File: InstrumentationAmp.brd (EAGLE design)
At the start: 21 x 23.5 mm, 14 parts, among them IC1 AD623R

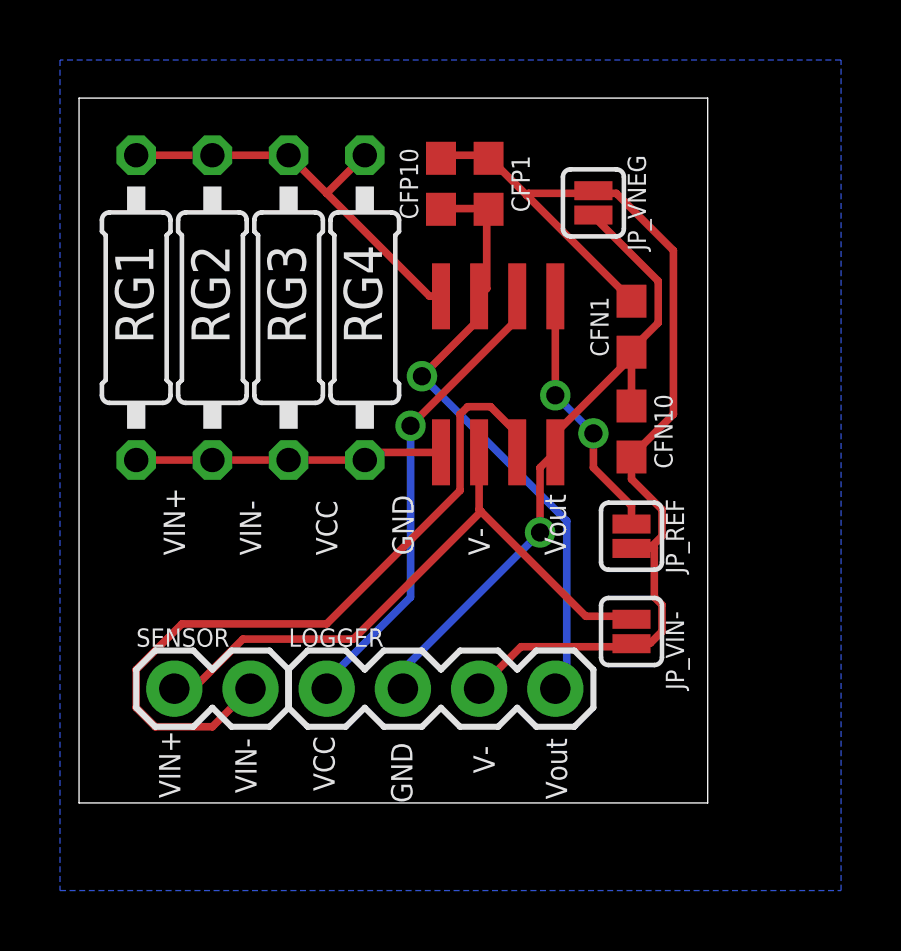
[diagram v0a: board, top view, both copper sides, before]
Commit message: Names match README; connect Vref
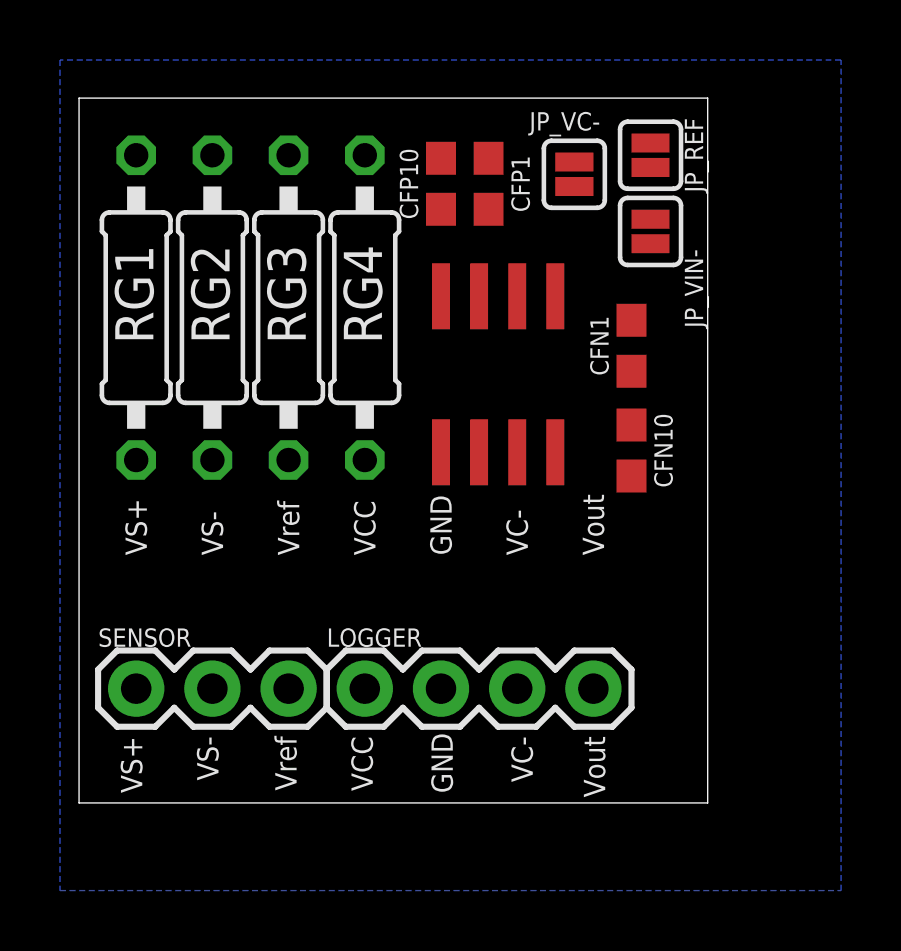
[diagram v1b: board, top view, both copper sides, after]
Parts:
- removed JP_VNEG: (no value), SparkFun-Jumpers:SMT-JUMPER_2_NC_PASTE_SILK
- added JP_VC-: (no value), SparkFun-Jumpers:SMT-JUMPER_2_NC_PASTE_SILK
- SENSOR: device SparkFun-Connectors:1X02 -> SparkFun-Connectors:1X03
- moved JP_VIN- 13.4 mm to (19.1, 19.1)
- moved JP_REF 12.7 mm to (19.1, 21.6)
- moved SENSOR 1.27 mm to (1.91, 3.81)
- moved LOGGER 1.27 mm to (9.53, 3.81)
- moved CFN1 0.63 mm to (18.4, 15.2)
- moved CFN10 0.63 mm to (18.4, 11.7)
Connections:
- removed net N$3: IC1.5, JP_REF.2
- removed net VIN+: IC1.3, SENSOR.2
- removed net VIN-: IC1.2, JP_VIN-.2, SENSOR.1
- new net VREF: IC1.5, JP_REF.2, SENSOR.1
- new net VS+: IC1.3, SENSOR.3
- new net VS-: IC1.2, JP_VIN-.2, SENSOR.2
- net GND: now also JP_VC-.1; no longer JP_VNEG.1
- net VNEG: now also JP_VC-.2; no longer JP_VNEG.2
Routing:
- net GND: track 36.0 -> 0.00 mm
- net VIN+: track 24.7 -> 0.00 mm
- net VNEG: track 21.9 -> 0.00 mm, vias 1 -> 0
- net VIN-: track 21.2 -> 0.00 mm
- net VCC: track 20.7 -> 0.00 mm, vias 1 -> 0
- net VOUT: track 15.7 -> 0.00 mm, vias 1 -> 0
- net RG-B: track 13.9 -> 0.00 mm
- net RG-A: track 10.3 -> 0.00 mm
- net N$3: track 8.64 -> 0.00 mm, vias 2 -> 0
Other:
- board text added: "VC-"
- board text added: "VS+"
- board text added: "VS-"
- board text added: "Vref"
- board text removed: "V-"
- board text removed: "VIN+"
- board text removed: "VIN-"

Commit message: ERC, DRC
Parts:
- moved SENSOR 0.95 mm to (2.86, 3.81)
- moved LOGGER 0.95 mm to (10.5, 3.81)
- moved CFN1 0.63 mm to (18.4, 15.9)
- moved CFN10 0.63 mm to (18.4, 12.4)
- renumbered JP_VIN- to JP_VS-
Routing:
- net VREF: track 0.00 -> 28.7 mm, vias 0 -> 1
- net GND: track 0.00 -> 24.6 mm, vias 0 -> 2
- net VS-: track 0.00 -> 22.4 mm
- net VNEG: track 0.00 -> 22.3 mm, vias 0 -> 2
- net VCC: track 0.00 -> 22.0 mm, vias 0 -> 1
- net VOUT: track 0.00 -> 14.8 mm, vias 0 -> 1
- net RG-B: track 0.00 -> 13.9 mm
- net VS+: track 0.00 -> 10.7 mm
- net RG-A: track 0.00 -> 10.3 mm
